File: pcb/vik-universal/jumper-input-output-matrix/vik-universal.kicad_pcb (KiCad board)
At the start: 2 copper layers, 44.5 x 43 mm, 150 parts, among them J1001 Conn_01x01_Socket

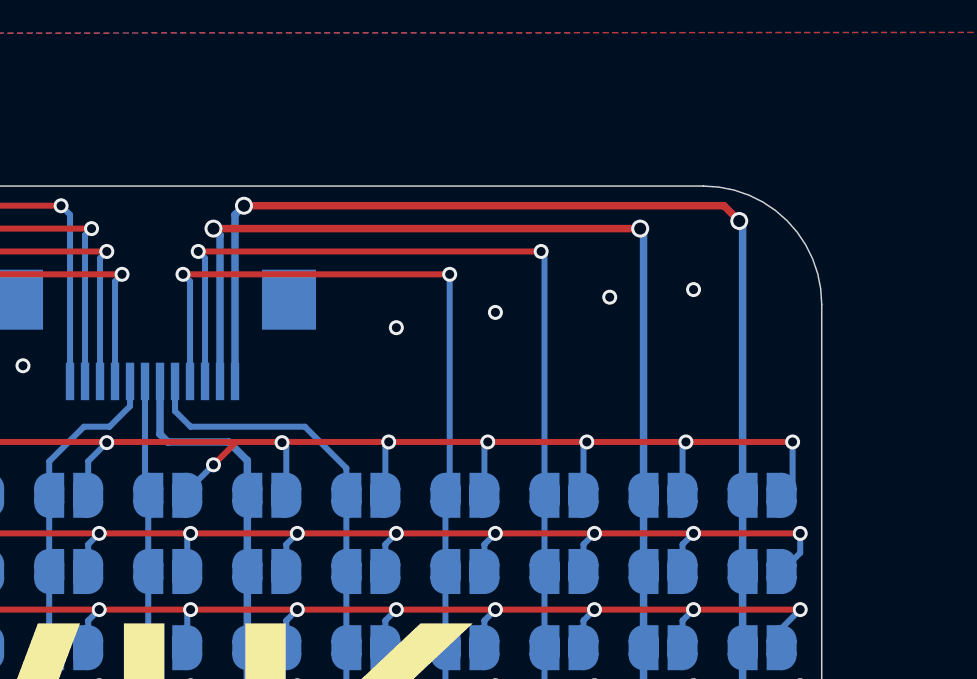
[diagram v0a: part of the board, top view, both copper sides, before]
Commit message: vik universal jumper input output matrix - added I2C pull ups, jumpers to enable or disable I2C pull up resistors
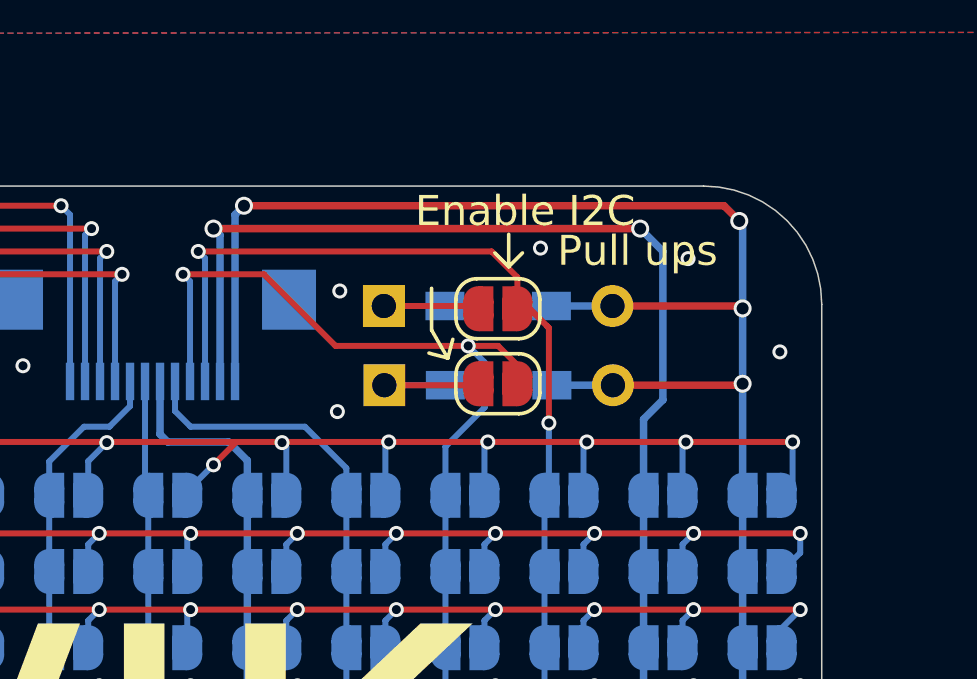
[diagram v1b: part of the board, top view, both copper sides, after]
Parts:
- added JP1145: SolderJumper_2_Open, Jumper:SolderJumper-2_P1.3mm_Open_RoundedPad1.0x1.5mm, F.Cu at (102.8, 92.8)
- added JP1146: SolderJumper_2_Open, Jumper:SolderJumper-2_P1.3mm_Open_RoundedPad1.0x1.5mm, F.Cu at (102.8, 90.3)
- added R1001: 4.7k, local:D3_TH_SMD, B.Cu at (102.8, 92.8)
- added R1002: 4.7k, local:D3_TH_SMD, B.Cu at (102.8, 90.2)
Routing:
- net VDD_3.3V: track 59.8 -> 72.6 mm, vias 2 -> 4
- net Net-(JP1146-B): track 0.00 -> 5.22 mm
- net Net-(JP1145-B): track 0.00 -> 5.19 mm
- net SCL: track 47.9 -> 50.4 mm
- net SDA: track 52.0 -> 51.4 mm
- net GND: track 56.3 -> 56.8 mm, vias 10 -> 11
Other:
- board text added: "Enable I2C"
- board text added: "Pull ups"
